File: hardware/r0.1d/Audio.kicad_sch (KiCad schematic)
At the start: 85 parts, among them IC1 LM4861M, J1 Kenwood-2.5, J11 Radio_Opt, J4 CAT_TX, J5 Kenwood-3.5, J6 CAT_TX, J7 Radio, Q1 IRLML2060, Q2 BSS138, Q3 BSS138, U1 MAX9814, U6 MCP6002, U7 MCP6002, U8 MCP4551-103, U9 MCP4551-104

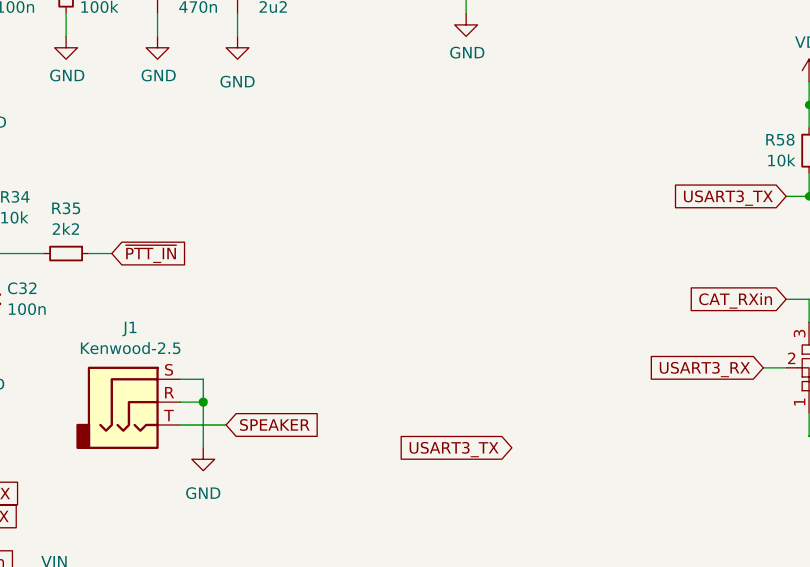
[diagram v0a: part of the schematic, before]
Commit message: Update r0.1d
Added speaker connector, beautified silk screen
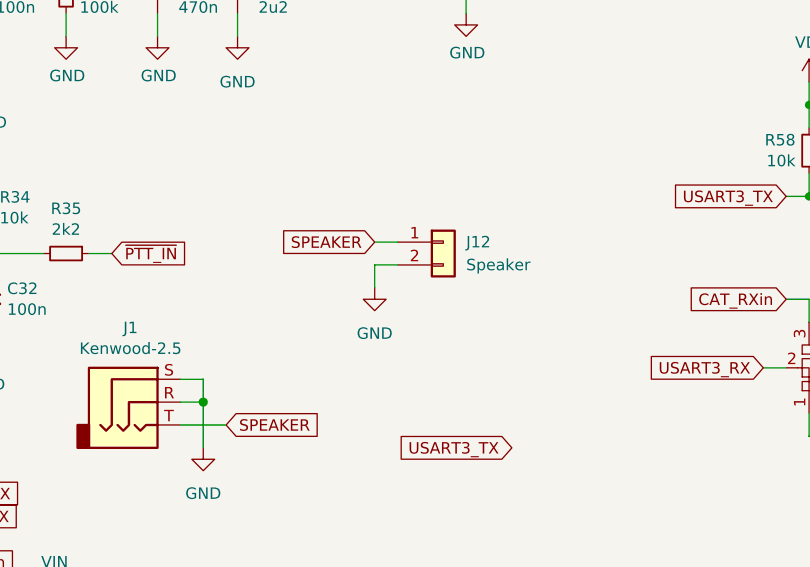
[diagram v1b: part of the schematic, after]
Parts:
- added J12: Speaker, Connector_PinHeader_2.54mm:PinHeader_1x02_P2.54mm_Vertical, symbol Connector_Generic:Conn_01x02
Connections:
- net GND: now also J12.2 (Pin_2)
- net SPEAKER: now also J12.1 (Pin_1)
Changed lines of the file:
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@@
     (stroke (width 0) (type solid) (color 0 0 0 0))
+  )
+  (wire (pts (xy 82.55 139.7) (xy 85.09 139.7))
+    (stroke (width 0) (type default) (color 0 0 0 0))
   )
   (wire (pts (xy 247.65 29.21) (xy 252.73 29.21))
@@
     (stroke (width 0) (type solid) (color 0 0 0 0))
   )
+  (wire (pts (xy 82.55 142.24) (xy 82.55 139.7))
+    (stroke (width 0) (type default) (color 0 0 0 0))
+  )
   (wire (pts (xy 133.35 27.94) (xy 133.35 30.48))
     (stroke (width 0) (type solid) (color 0 0 0 0))
@@
   )
   (wire (pts (xy 130.81 121.92) (xy 130.81 124.46))
+    (stroke (width 0) (type default) (color 0 0 0 0))
+  )
+  (wire (pts (xy 82.55 137.16) (xy 85.09 137.16))
     (stroke (width 0) (type default) (color 0 0 0 0))
   )
@@
     (property "Intersheet References" "${INTERSHEET_REFS}" (id 0) (at 152.0618 124.5394 0)
       (effects (font (size 1.27 1.27)) (justify right) hide)
+    )
+  )
+  (global_label "SPEAKER" (shape input) (at 82.55 137.16 180) (fields_autoplaced)
+    (effects (font (size 1.27 1.27)) (justify right))
+    (property "Intersheet References" "${INTERSHEET_REFS}" (id 0) (at 115.57 297.18 0)
+      (effects (font (size 1.27 1.27)) hide)
     )
   )
@@
     (pin "1")
   )
+  (symbol (lib_id "power:GND") (at 82.55 142.24 0) (unit 1)
+    (in_bom yes) (on_board yes)
+    (property "Reference" "#PWR083" (id 0) (at 82.55 148.59 0)
+      (effects (font (size 1.27 1.27)) hide)
+    )
+    (property "Value" "GND" (id 1) (at 82.55 147.32 0))
+    (property "Footprint" "" (id 2) (at 82.55 142.24 0)
+      (effects (font (size 1.27 1.27)) hide)
+    )
+    (property "Datasheet" "" (id 3) (at 82.55 142.24 0)
+      (effects (font (size 1.27 1.27)) hide)
+    )
+    (pin "1")
+  )
   (symbol (lib_id "pkl_device:pkl_C_Small") (at 58.42 109.22 0) (unit 1)
     (in_bom yes) (on_board yes) (fields_autoplaced)
@@
     )
     (pin "1")
+    (pin "2")
+  )
+  (symbol (lib_id "Connector_Generic:Conn_01x02") (at 90.17 137.16 0) (unit 1)
+    (in_bom yes) (on_board yes) (fields_autoplaced)
+    (property "Reference" "J12" (id 0) (at 92.71 137.1599 0)
+      (effects (font (size 1.27 1.27)) (justify left))
+    )
+    (property "Value" "Speaker" (id 1) (at 92.71 139.6999 0)
+      (effects (font (size 1.27 1.27)) (justify left))
+    )
+    (property "Footprint" "Connector_PinHeader_2.54mm:PinHeader_1x02_P2.54mm_Vertical" (id 2) (at 90.17 137.16 0)
+      (effects (font (size 1.27 1.27)) hide)
+    )
+    (property "Datasheet" "~" (id 3) (at 90.17 137.16 0)
+      (effects (font (size 1.27 1.27)) hide)
+    )
+    (pin "1")
